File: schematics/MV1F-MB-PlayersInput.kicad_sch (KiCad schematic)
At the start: 46 parts

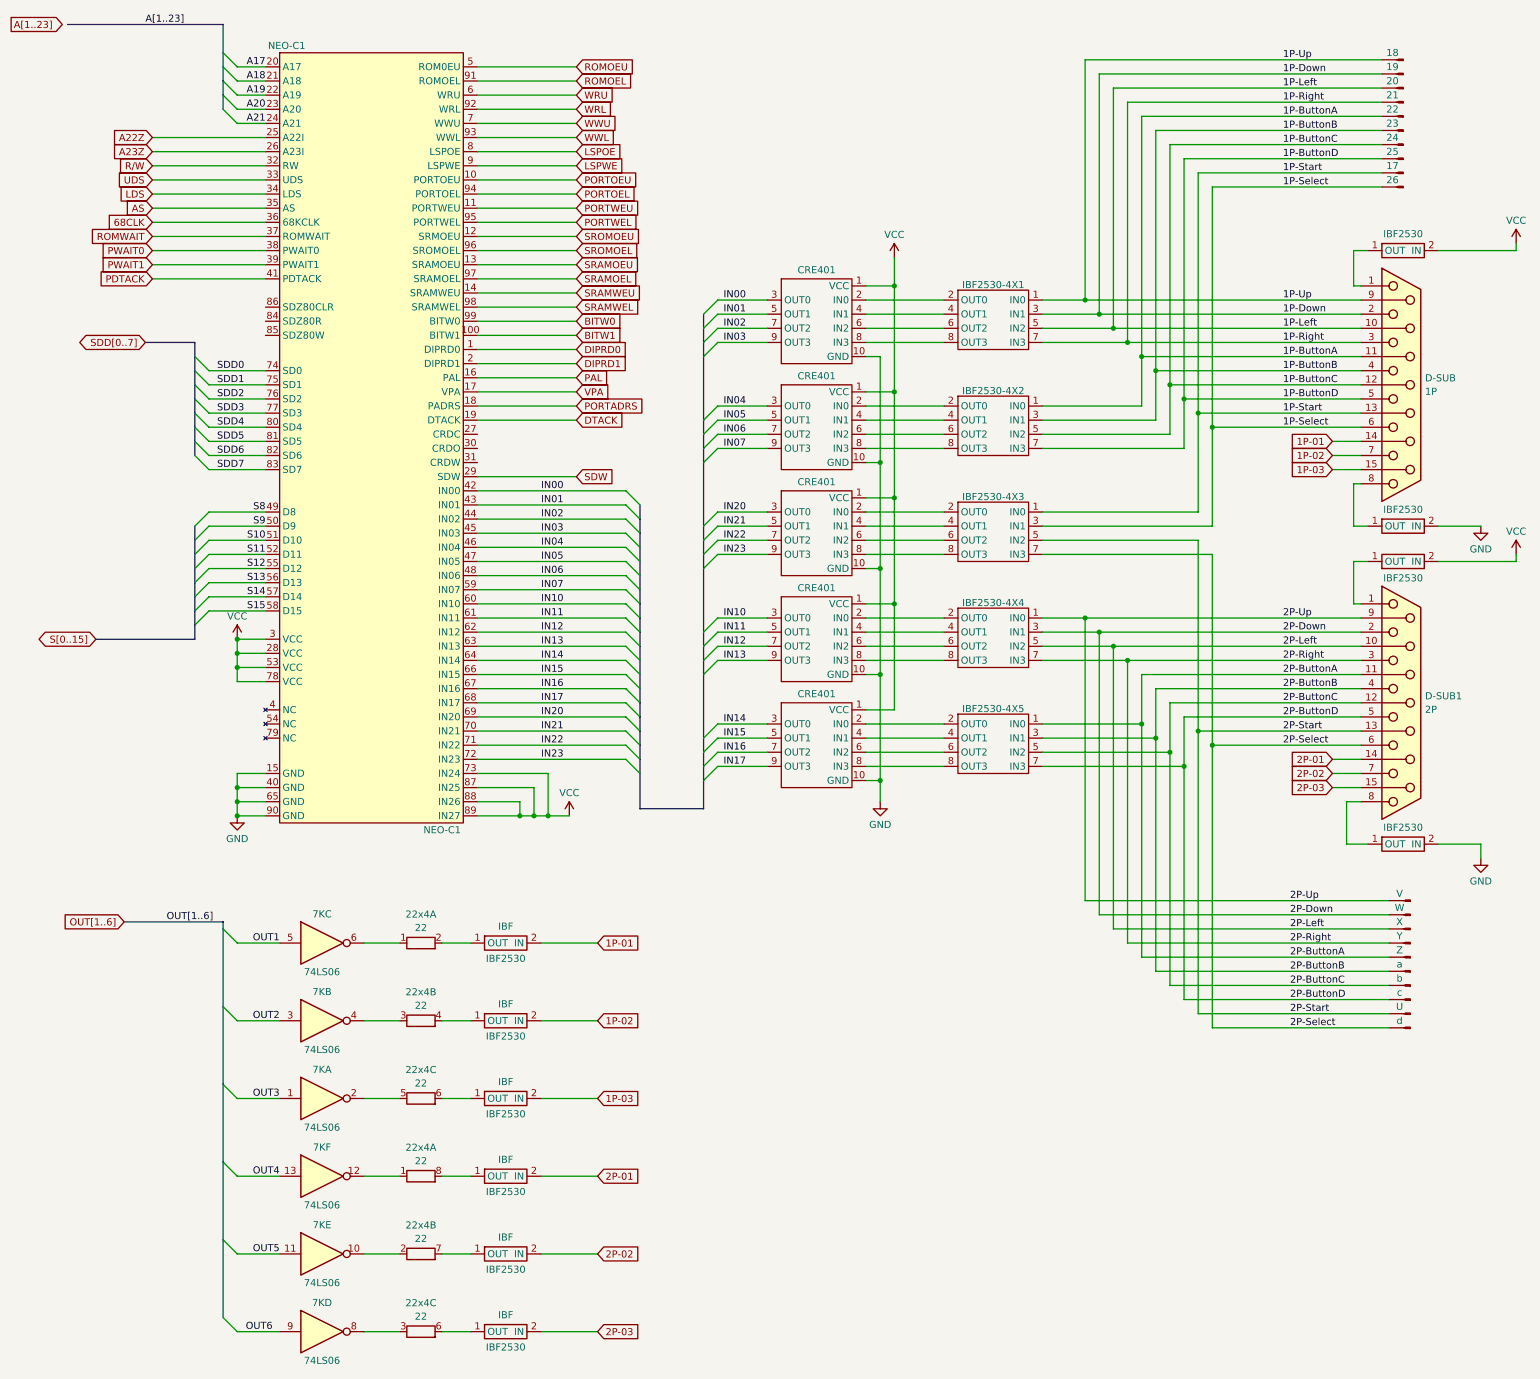
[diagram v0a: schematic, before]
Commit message: complete DaughterBoard
rename sub files
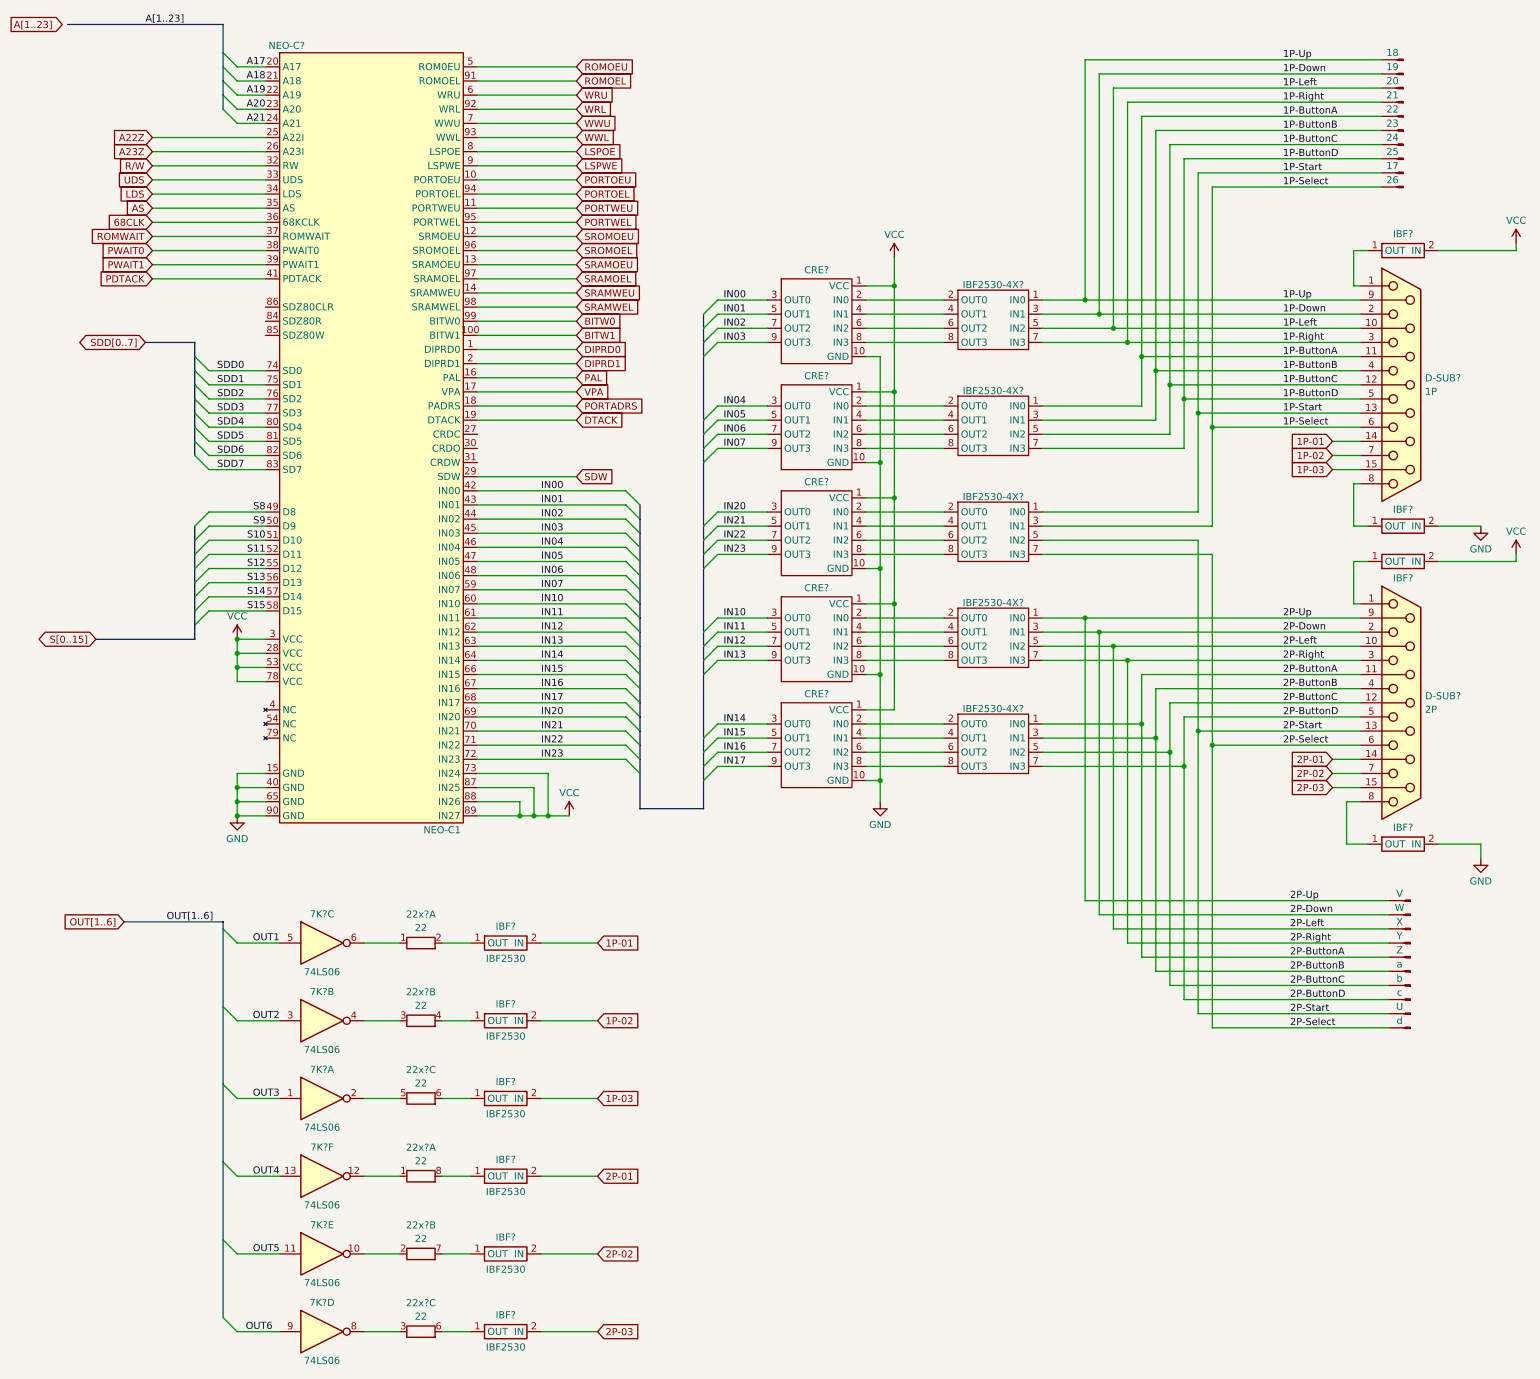
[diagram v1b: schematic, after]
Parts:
- renumbered 22x4 to 22x?, 7K to 7K?, CRE401 to CRE?, D-SUB to D-SUB?, D-SUB1 to D-SUB?, IBF2530-4X2 to IBF2530-4X?, IBF2530-4X5 to IBF2530-4X?, IBF2530-4X3 to IBF2530-4X?, IBF2530-4X1 to IBF2530-4X?, IBF2530-4X4 to IBF2530-4X?, IBF2530 to IBF?, IBF to IBF?, NEO-C1 to NEO-C?

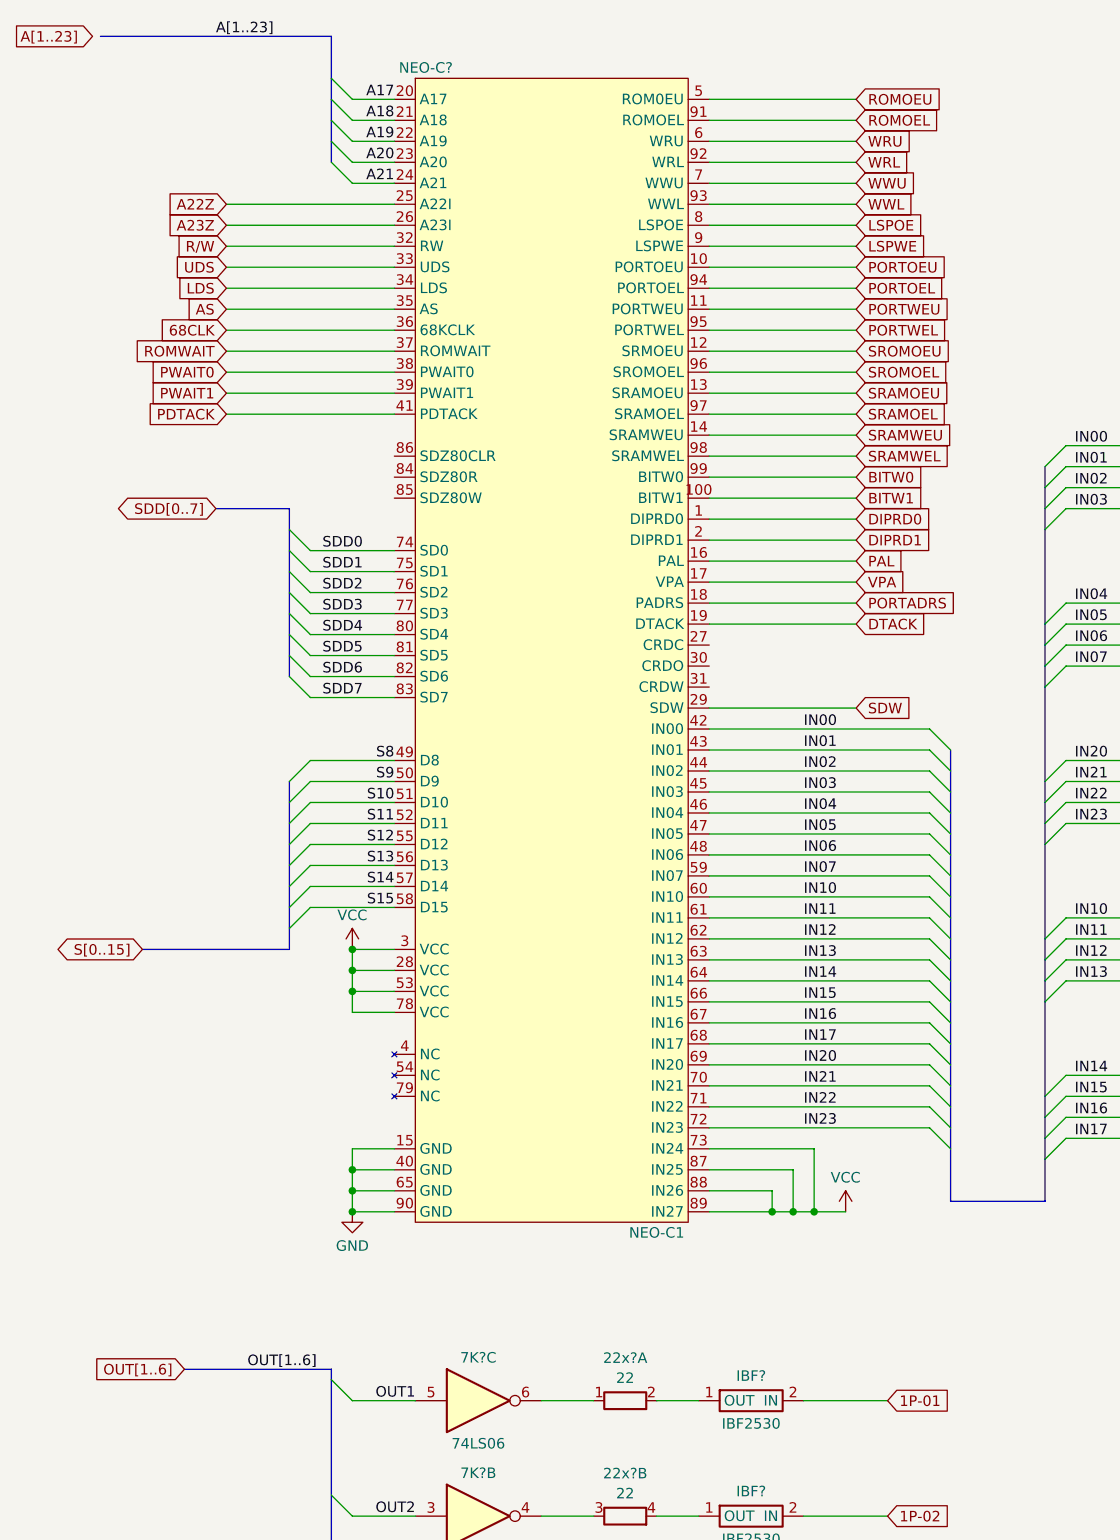
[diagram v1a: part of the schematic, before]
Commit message: Typo... and orphan labels remove
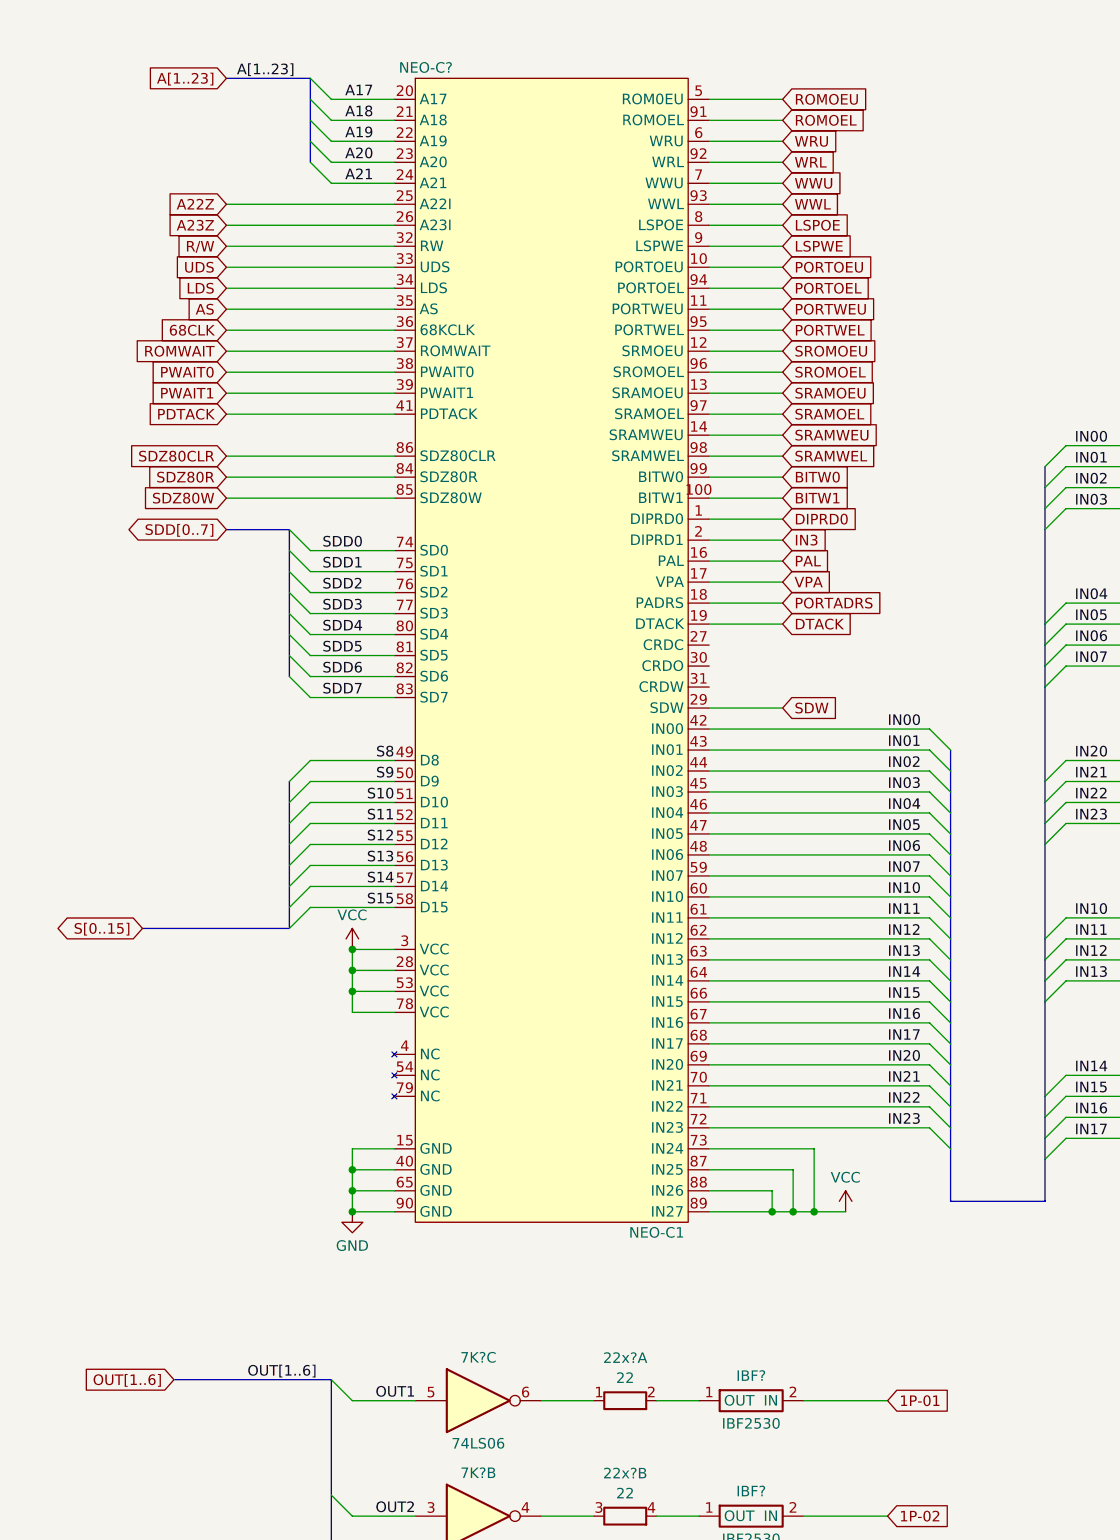
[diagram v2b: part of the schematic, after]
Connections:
- net SDZ80R: now reaches NEO-C?.84 (SDZ80R)
- net SDZ80W: now reaches NEO-C?.85 (SDZ80W)
- net SDZ80CLR: now reaches NEO-C?.86 (SDZ80CLR)
- net DIPRD1 renamed IN3

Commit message: Typo
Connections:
- net SRAMOEL renamed BRAMOEL
- net SRAMOEU renamed BRAMOEU
- net SRAMWEL renamed BRAMWEL
- net SRAMWEU renamed BRAMWEU
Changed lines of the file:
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@@
     )
   )
-  (global_label "SRAMWEL" (shape input) (at 109.22 67.31 0) (fields_autoplaced)
-    (effects (font (size 1.27 1.27)) (justify left))
-    (property "Intersheetrefs" "${INTERSHEET_REFS}" (at 120.8532 67.31 0)
+  (global_label "BRAMWEL" (shape input) (at 109.22 67.31 0) (fields_autoplaced)
+    (effects (font (size 1.27 1.27)) (justify left))
+    (property "Intersheetrefs" "${INTERSHEET_REFS}" (at 120.9137 67.31 0)
       (effects (font (size 1.27 1.27)) (justify left))
     )
@@
     )
   )
-  (global_label "SRAMOEU" (shape input) (at 109.22 59.69 0) (fields_autoplaced)
-    (effects (font (size 1.27 1.27)) (justify left))
-    (property "Intersheetrefs" "${INTERSHEET_REFS}" (at 121.0347 59.69 0)
+  (global_label "BRAMOEU" (shape input) (at 109.22 59.69 0) (fields_autoplaced)
+    (effects (font (size 1.27 1.27)) (justify left))
+    (property "Intersheetrefs" "${INTERSHEET_REFS}" (at 121.0952 59.69 0)
       (effects (font (size 1.27 1.27)) (justify left))
     )
@@
     )
   )
-  (global_label "SRAMOEL" (shape input) (at 109.22 62.23 0) (fields_autoplaced)
-    (effects (font (size 1.27 1.27)) (justify left))
-    (property "Intersheetrefs" "${INTERSHEET_REFS}" (at 120.7323 62.23 0)
+  (global_label "BRAMOEL" (shape input) (at 109.22 62.23 0) (fields_autoplaced)
+    (effects (font (size 1.27 1.27)) (justify left))
+    (property "Intersheetrefs" "${INTERSHEET_REFS}" (at 120.7928 62.23 0)
       (effects (font (size 1.27 1.27)) (justify left))
     )
@@
     )
   )
-  (global_label "SRAMWEU" (shape input) (at 109.22 64.77 0) (fields_autoplaced)
-    (effects (font (size 1.27 1.27)) (justify left))
-    (property "Intersheetrefs" "${INTERSHEET_REFS}" (at 121.1556 64.77 0)
-      (effects (font (size 1.27 1.27)) (justify left))
-    )
+  (global_label "BRAMWEU" (shape input) (at 109.22 64.77 0) (fields_autoplaced)
+    (effects (font (size 1.27 1.27)) (justify left))
+    (property "Intersheetrefs" "${INTERSHEET_REFS}" (at 121.2161 64.77 0)
+      (effects (font (size 1.27 1.27)) (justify left))
+    )
